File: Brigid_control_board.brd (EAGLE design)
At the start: 53.3 x 53.3 mm, 28 parts, among them J1 ARDUINO_R3_SHIELD, P1 39-30-02?, P2 39-30-02?, P3 39-30-02?, P4 39-30-02?, P5 39-30-02?, P6 39-30-02?, P7 39-30-02?, Q1 T460, Q2 T460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

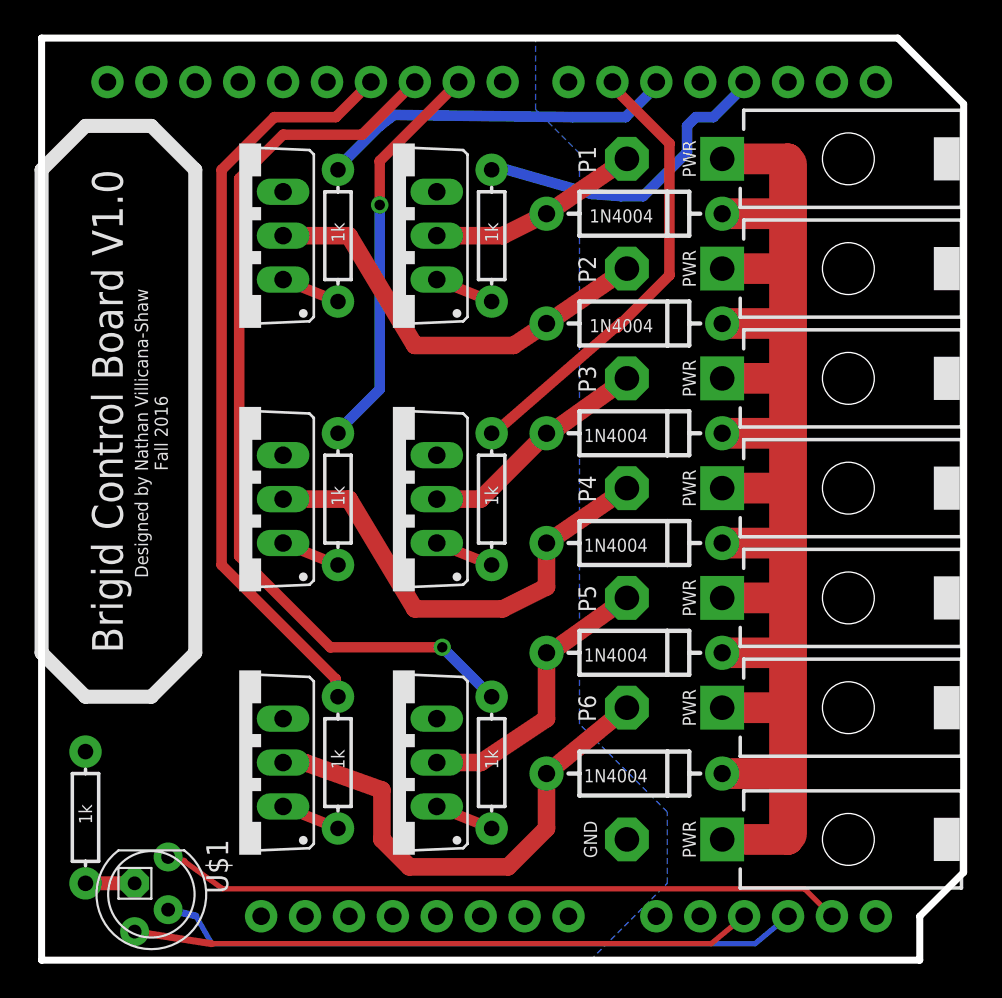
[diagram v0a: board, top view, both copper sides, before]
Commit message: made brigid rev 2, created LED version of code
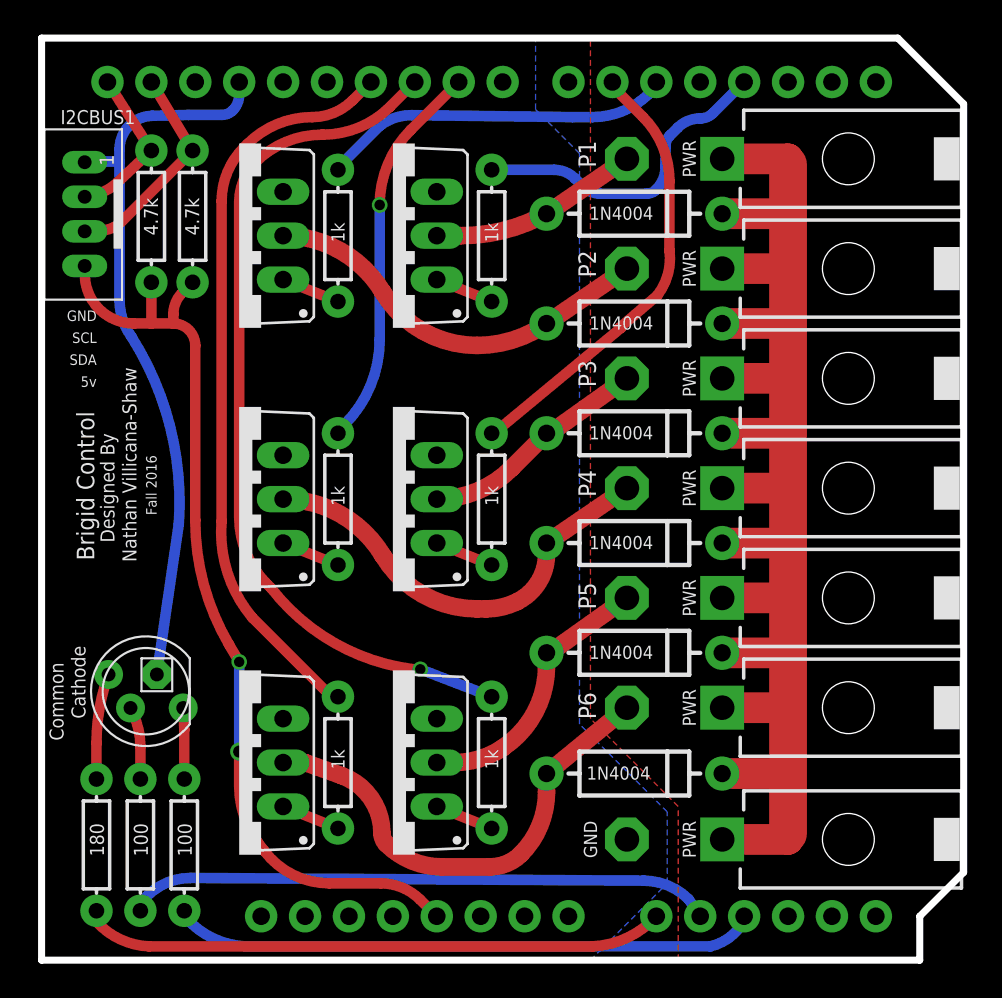
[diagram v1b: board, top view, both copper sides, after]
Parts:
- added I2CBUS1: JST-PH_4-PIN_HEADER, JST_connectors:JST_B4B-PH_HEADER
- added R10, R11: 4.7k, SparkFun-Passives:AXIAL-0.3EZ
- added R8: 100, SparkFun-Passives:AXIAL-0.3EZ
- added R9: 180, SparkFun-Passives:AXIAL-0.3EZ
- P1, P2, P3, P4, P5, P6, P7: value 39-30-02? -> Molex Mini-Fit Jr.
- R1: value 1k -> 100
- U$1: value RGBLED_CA -> RGB LED
- moved U$1 11.8 mm to (6.03, 15.6), turned to 180 degrees
- moved R1 5.93 mm to (8.26, 6.67)
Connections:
- new net N$1: J1.A0, R9.P$2
- new net N$17: I2CBUS1.P4, J1.5V, R10.P$1, R11.P$1
- new net N$20: I2CBUS1.P1, J1.GND@2, U$1.2
- new net N$7: R1.P$1, U$1.1
- new net SCL: I2CBUS1.P2, J1.SCL, R10.P$2
- new net SDA: I2CBUS1.P3, J1.SDA, R11.P$2
- net GND: no longer R1.P$1
- net N$2: now also J1.A1, R8.P$2; no longer J1.A2, U$1.4
- net N$4: now also J1.A2, R1.P$2; no longer J1.A4, U$1.1
- net N$5: now also R9.P$1, U$1.4; no longer J1.A3, U$1.3
- net N$8: now also R8.P$1, U$1.3; no longer R1.P$2, U$1.2
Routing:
- net N$17: track 0.00 -> 54.7 mm, vias 0 -> 2
- net N$20: track 0.00 -> 42.1 mm
- net N$1: track 0.00 -> 33.7 mm
- net N$5: track 37.4 -> 6.11 mm
- net SDA: track 0.00 -> 12.7 mm
- net PWR: track 105.6 -> 94.0 mm
- net SCL: track 0.00 -> 9.49 mm
- net N$4: track 39.6 -> 33.9 mm
- net N$7: track 0.00 -> 4.11 mm
- net N$16: track 27.3 -> 24.8 mm
- net D10: track 52.3 -> 50.0 mm
- net N$10: track 24.8 -> 22.7 mm
- net N$2: track 35.9 -> 33.9 mm
- net N$22: track 29.1 -> 27.4 mm
- net N$8: track 2.84 -> 4.19 mm
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- added copper zone on layer 1, net GND
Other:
- board text added: "5v"
- board text added: "Brigid Control"
- board text added: "Cathode"
- board text added: "Common"
- board text added: "Designed By"
- board text added: "Fall 2016"
- board text added: "Nathan Villicana-Shaw"
- board text added: "SCL"
- board text added: "SDA"
- board text removed: "Brigid Control Board V1.0"
- board text removed: "Designed by Nathan Villicana-Shaw Fall 2016"
